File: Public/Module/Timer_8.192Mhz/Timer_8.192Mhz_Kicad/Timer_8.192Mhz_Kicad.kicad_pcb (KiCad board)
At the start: 2 copper layers, 30.5 x 76.2 mm, 13 parts, among them J1 Power_Input, J2 Signal_Output, U1 DIP-14, U2 LP2985-3.3

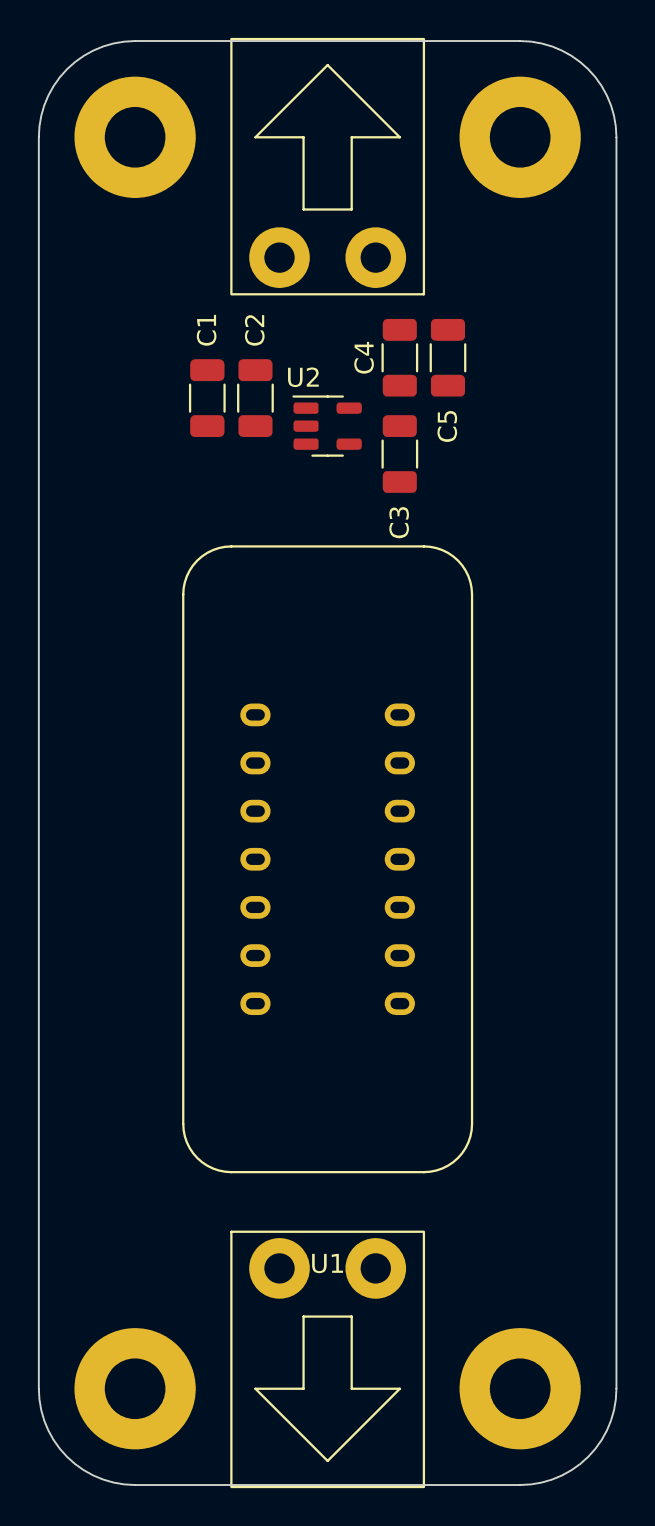
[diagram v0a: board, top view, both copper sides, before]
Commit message: Update 8.192Mhz Timer
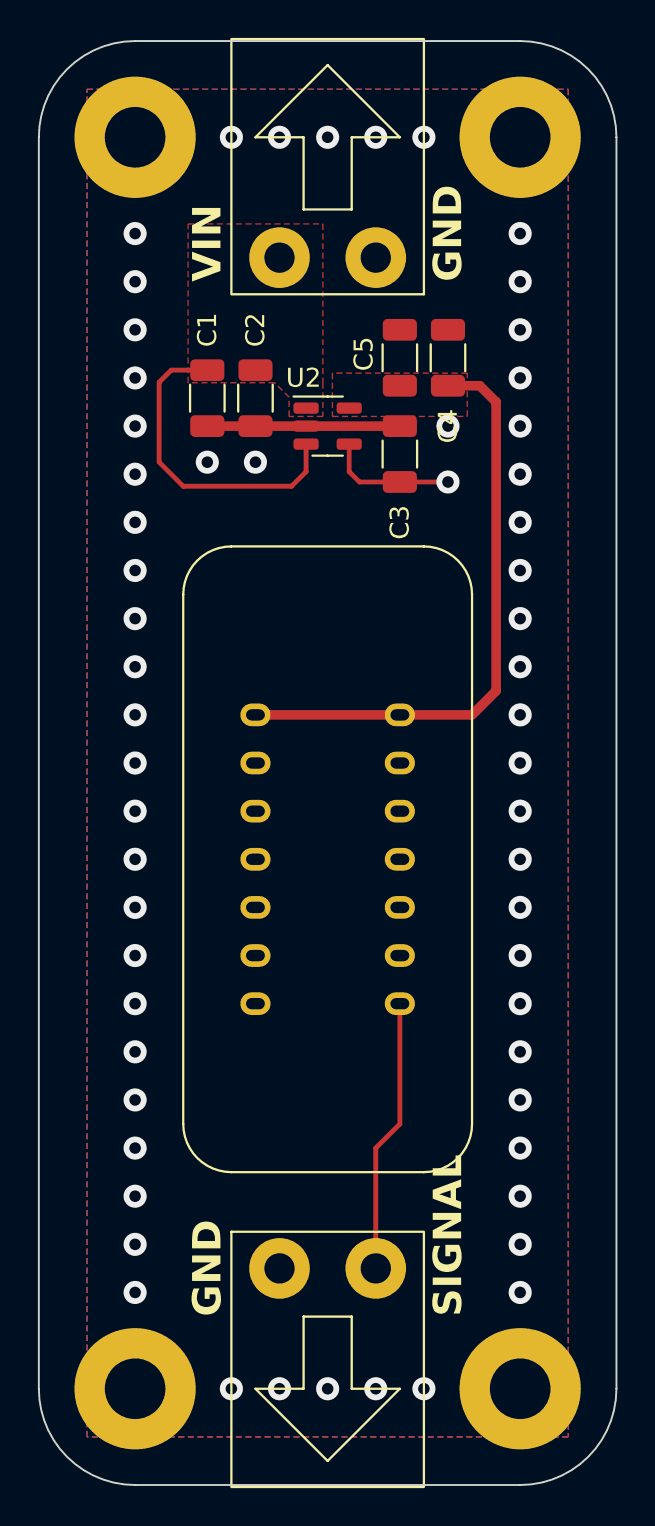
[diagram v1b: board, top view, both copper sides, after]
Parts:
- moved C4 2.54 mm to (95.2, 39.6)
- moved C5 2.54 mm to (92.7, 39.6)
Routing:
- net /VOUT: track 0.00 -> 31.4 mm
- net /VIN: track 0.00 -> 17.1 mm
- net /SIGNAL: track 0.00 -> 14.5 mm
- net GNDREF: track 0.00 -> 10.2 mm, vias 0 -> 59
- net Net-(U2-BP): track 0.00 -> 6.89 mm, vias 0 -> 1
- added copper zone on F.Cu, net /VIN
- added copper zone on F.Cu, net /VOUT
- added copper zone on B.Cu, net GNDREF
- added copper zone on F.Cu, net GNDREF
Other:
- board text added: "GND"
- board text added: "SIGNAL"
- board text added: "SOUT"
- board text added: "VIN"
